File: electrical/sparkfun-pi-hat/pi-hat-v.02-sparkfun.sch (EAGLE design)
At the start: 13 parts, among them J1 PIN20X2

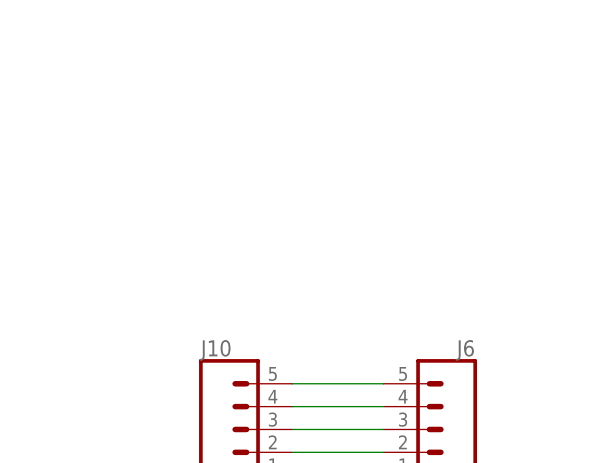
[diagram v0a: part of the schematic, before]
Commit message: plate through holes, upload BOM
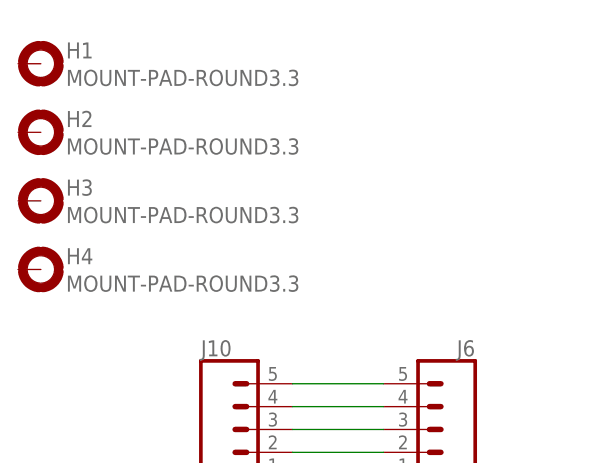
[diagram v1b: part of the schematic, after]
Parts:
- added H1, H2, H3, H4: MOUNT-PAD-ROUND3.3, holes:MOUNT-PAD-ROUND3.3
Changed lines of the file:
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@@
 <part name="J12" library="SparkFun-Connectors" deviceset="CONN_05" device=""/>
 <part name="J13" library="SparkFun-Connectors" deviceset="CONN_05" device=""/>
+<part name="H1" library="holes" deviceset="MOUNT-PAD-ROUND" device="3.3"/>
+<part name="H2" library="holes" deviceset="MOUNT-PAD-ROUND" device="3.3"/>
+<part name="H3" library="holes" deviceset="MOUNT-PAD-ROUND" device="3.3"/>
+<part name="H4" library="holes" deviceset="MOUNT-PAD-ROUND" device="3.3"/>
 </parts>
 <sheets>
@@
 <instance part="J12" gate="G$1" x="109.22" y="99.06"/>
 <instance part="J13" gate="G$1" x="109.22" y="78.74"/>
+<instance part="H1" gate="G$1" x="88.9" y="177.8"/>
+<instance part="H2" gate="G$1" x="88.9" y="170.18"/>
+<instance part="H3" gate="G$1" x="88.9" y="162.56"/>
+<instance part="H4" gate="G$1" x="88.9" y="154.94"/>
 </instances>
 <busses>
